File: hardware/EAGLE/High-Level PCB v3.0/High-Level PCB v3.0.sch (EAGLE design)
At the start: 57 parts, among them IC1 MCP2551, IC2 DS8921, IC3 DS8921, J1 Optical Mouse, J2 RaspπUart, J7 ODO_JACK, J8 DB9 Plug, J9 CAN Output, U1 COMPASS, U2 LLSHIFTER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

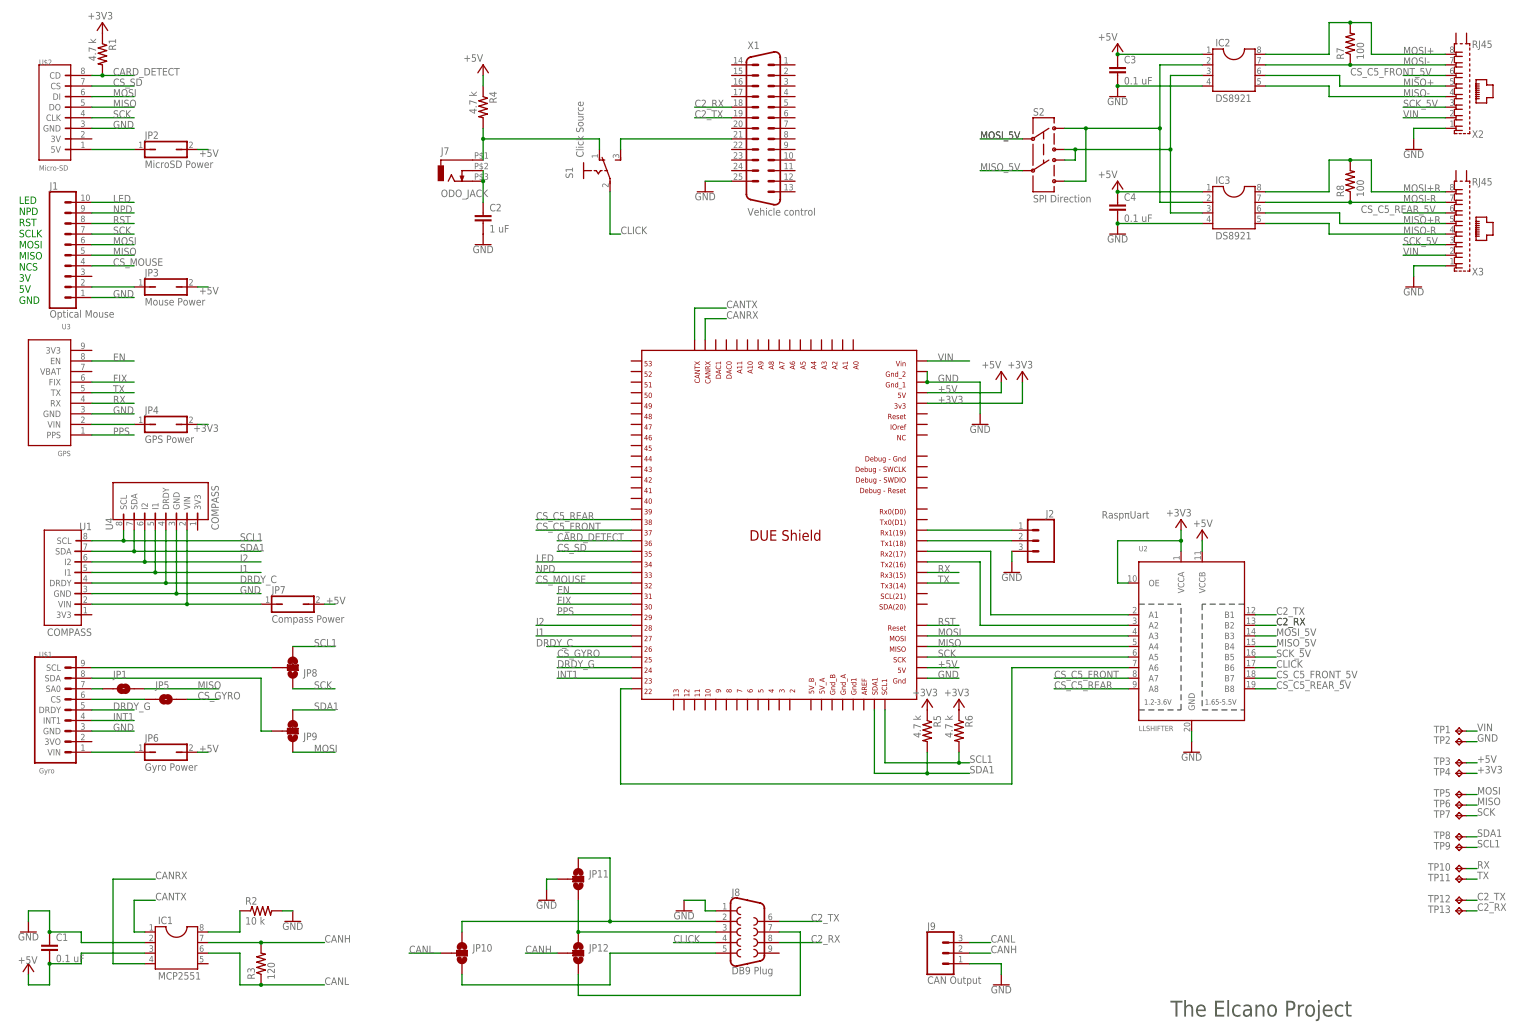
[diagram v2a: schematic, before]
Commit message: Added correct RJ45 footprints
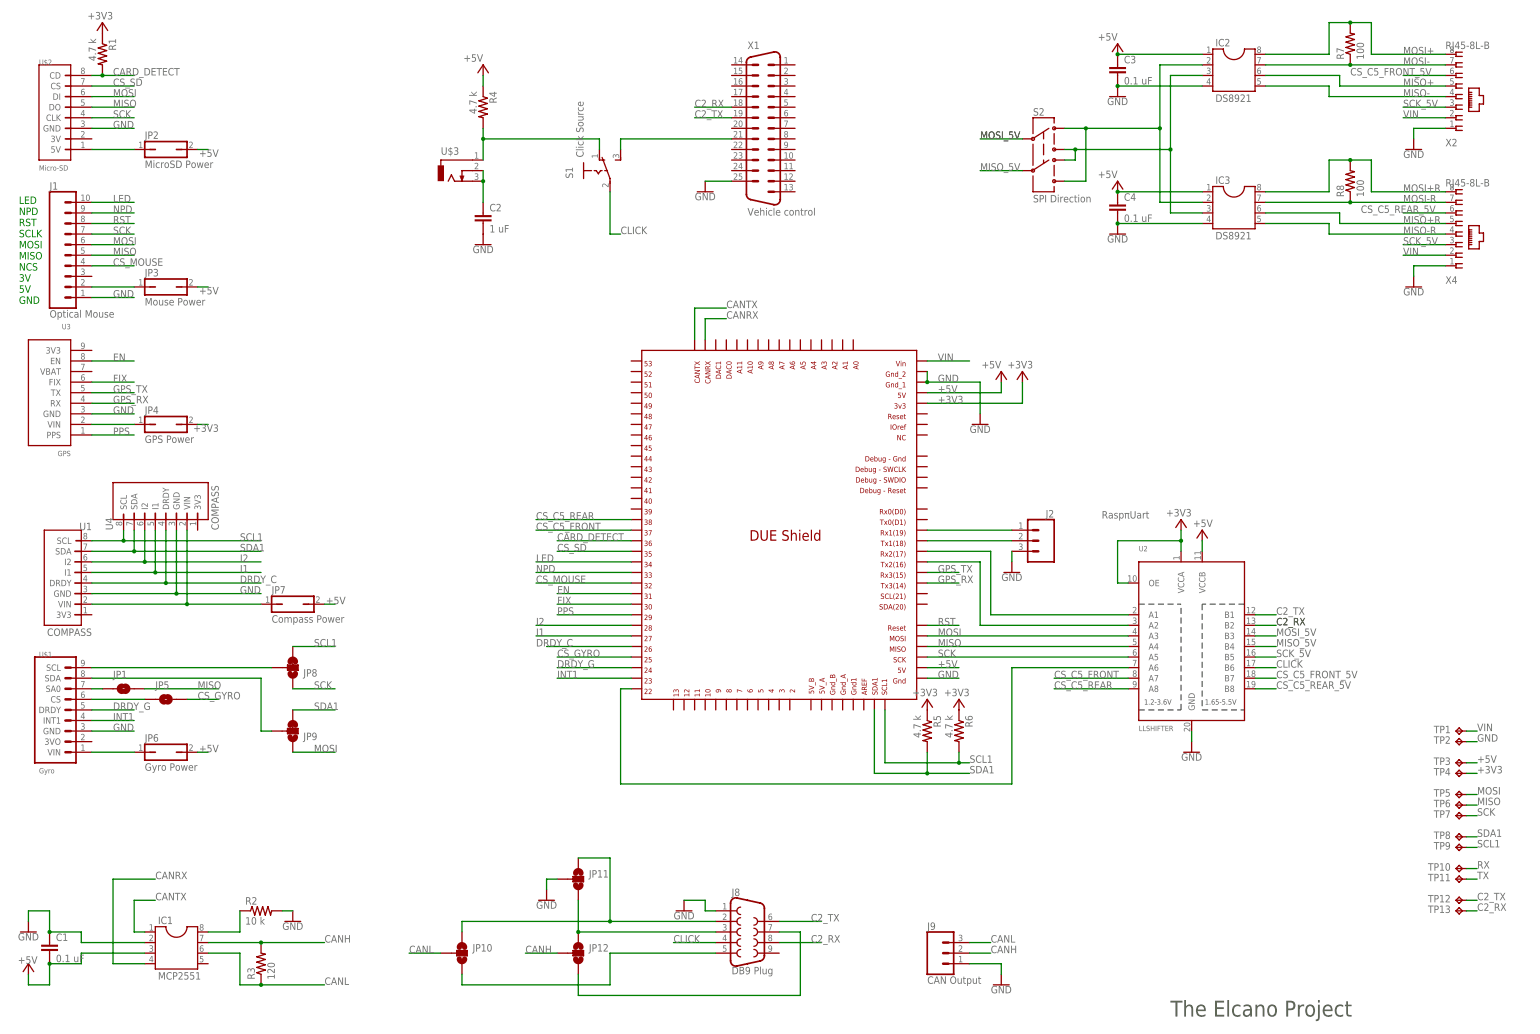
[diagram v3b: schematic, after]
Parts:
- removed J7: ODO_JACK, elcanoParts:ODO_JACK
- removed X3: RJ45, con-kycon:GLX-S-88M
- added U$3: (no value), ELCano_Footprints:2.5MMJACK
- added X4: RJ45-8L-B, con-tycoelectronics:RJ45-8L-B
- X2: value RJ45 -> RJ45-8L-B; device con-kycon:GLX-S-88M -> con-tycoelectronics:RJ45-8L-B
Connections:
- new net GPS_RX: MCU1.TX3, U3.RX
- new net GPS_TX: MCU1.RX3, U3.TX
- net CS_C5_REAR_5V: now also X4.6; no longer X3.6
- net GND: now also X4.1; no longer X3.1
- net MISO+R: now also X4.5; no longer X3.5
- net MISO-R: now also X4.4; no longer X3.4
- net MOSI+R: now also X4.8; no longer X3.8
- net MOSI-R: now also X4.7; no longer X3.7
- net N$1: now also U$3.2, U$3.3; no longer J7.2, J7.3
- net N$7: now also U$3.1; no longer J7.1
- net RX: no longer MCU1.RX3, U3.RX
- net SCK_5V: now also X4.3; no longer X3.3
- net TX: no longer MCU1.TX3, U3.TX
- net VIN: now also X4.2; no longer X3.2

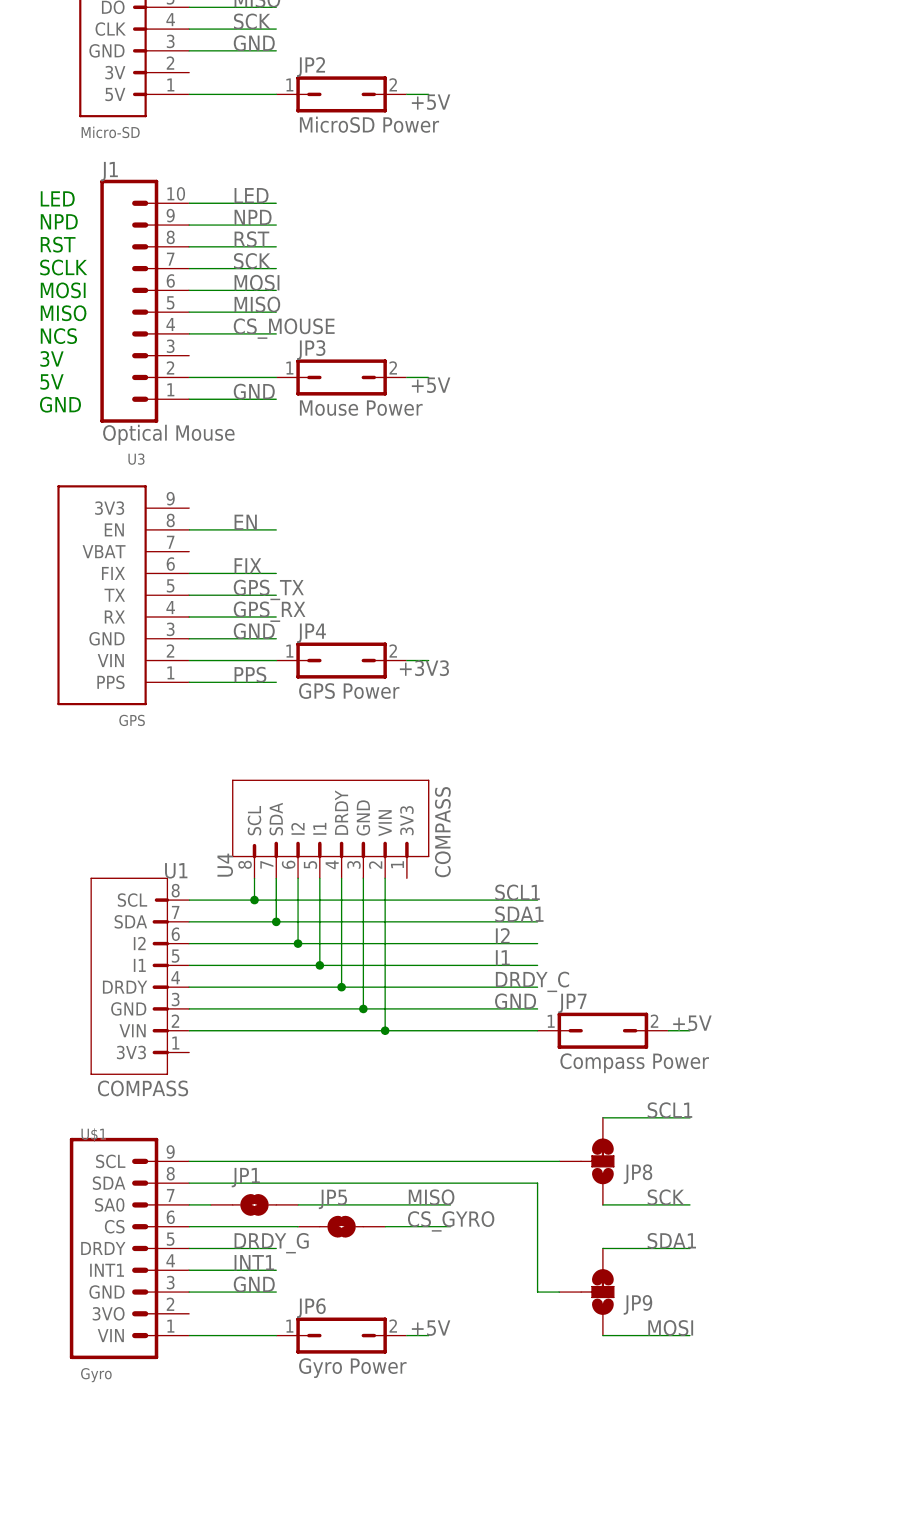
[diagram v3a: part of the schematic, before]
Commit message: Removed second Compass
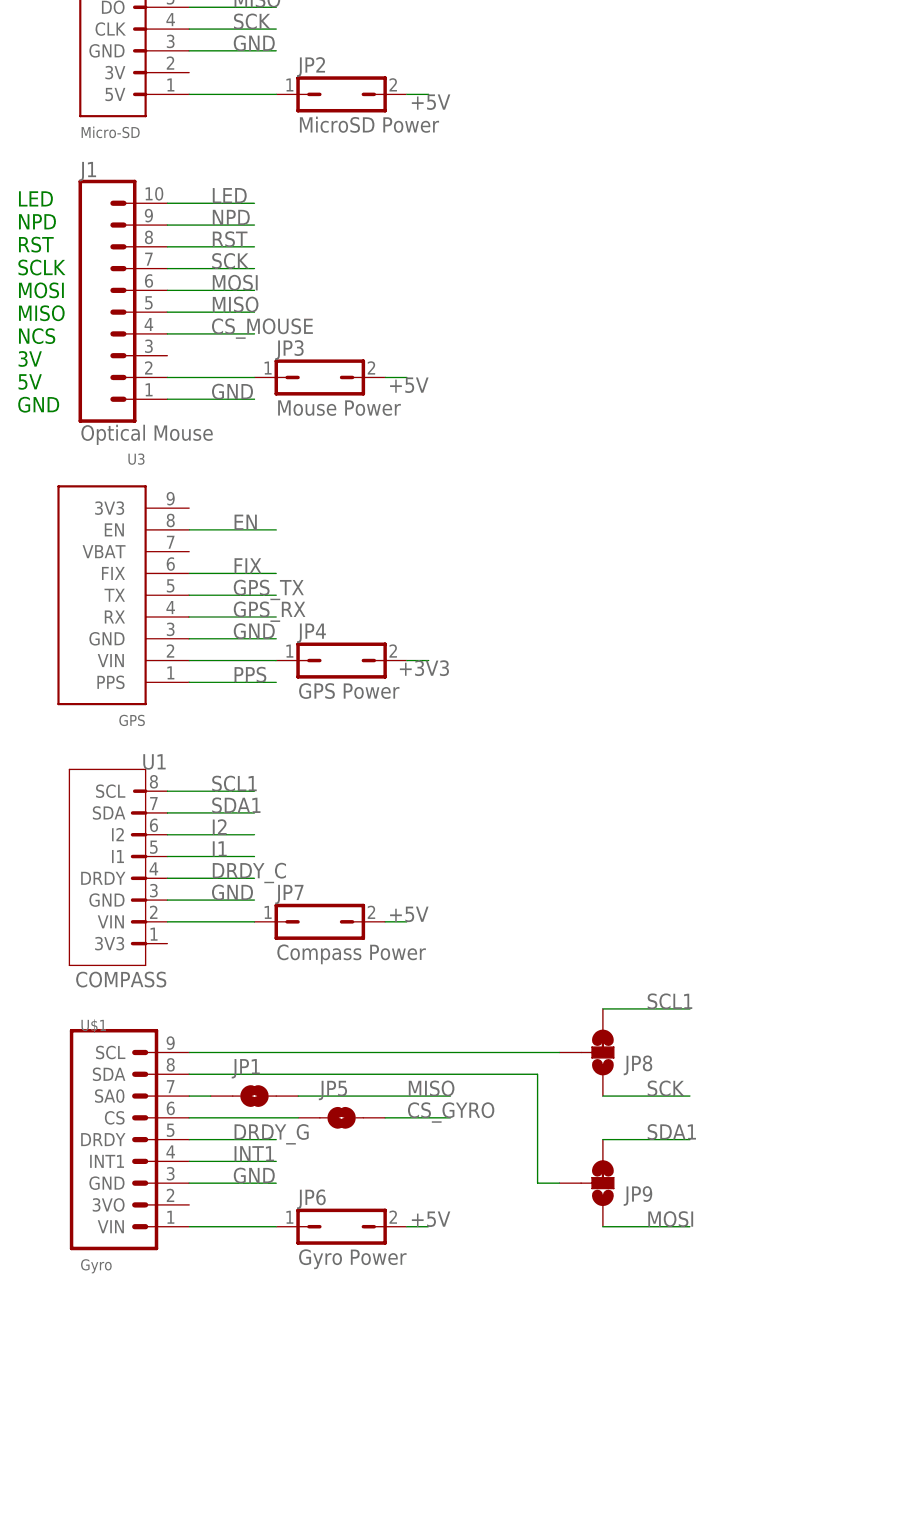
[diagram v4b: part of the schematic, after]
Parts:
- removed U4: COMPASS, ELCOMPASS:ELCOMPASS
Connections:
- net DRDY_C: no longer U4.DRDY
- net GND: no longer U4.GND
- net I1: no longer U4.I1
- net I2: no longer U4.I2
- net N$8: no longer U4.VIN
- net SCL1: no longer U4.SCL
- net SDA1: no longer U4.SDA
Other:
- moved on the sheet: J1, JP1, JP3, JP5, JP6, JP7, JP8, JP9, U$1, U1

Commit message: Add files via upload
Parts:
- removed S2: SPI Direction, elcanoParts:DPDT_DEV6X5MM_PAC
- added S3: SPI Direction, ELCano_Footprints:DPDT
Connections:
- net MISO_5V: now also S3.5; no longer S2.5
- net MOSI_5V: now also S3.2; no longer S2.2
- net N$2: now also S3.1, S3.6; no longer S2.1, S2.6
- net N$3: now also S3.3, S3.4; no longer S2.3, S2.4

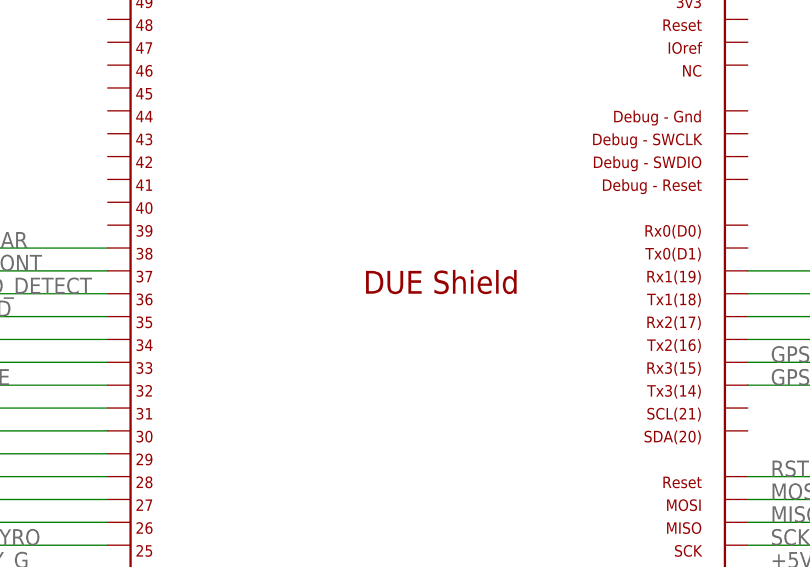
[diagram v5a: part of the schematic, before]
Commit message: changes
Changed DPDT. Updated with new Due library where the silk screen has been moved. 
Solved drill hole issue with Due library
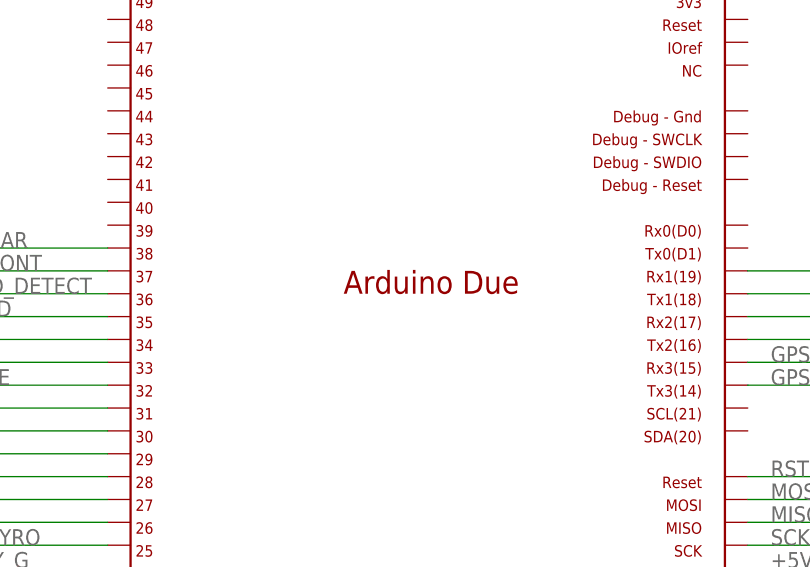
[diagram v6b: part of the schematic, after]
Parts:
- renumbered MCU1 to MCU2
